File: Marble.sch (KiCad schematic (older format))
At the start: 16 parts

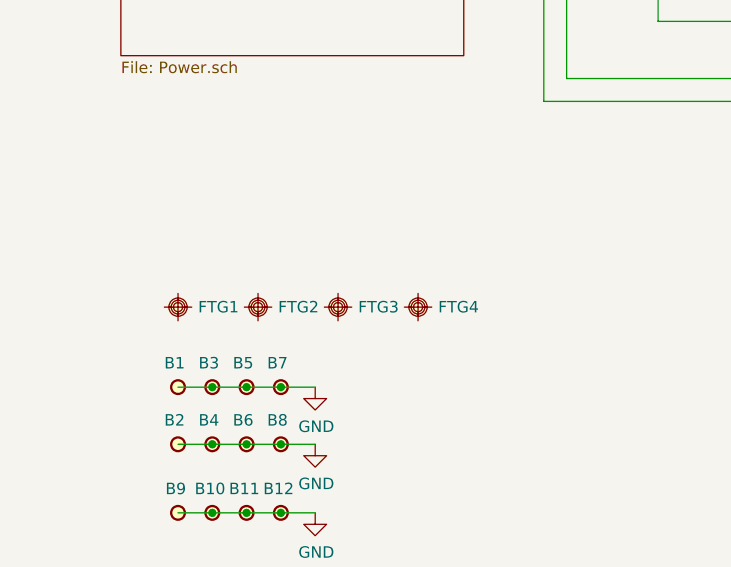
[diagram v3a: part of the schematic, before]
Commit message: 4 more fiducials
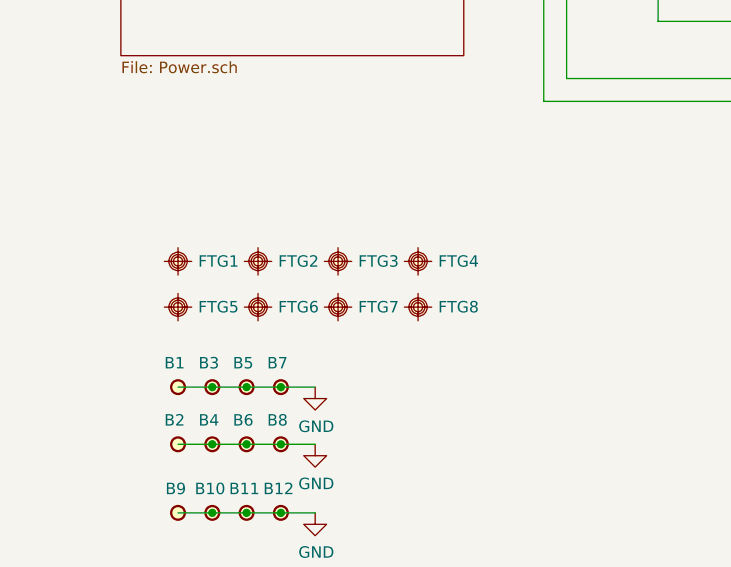
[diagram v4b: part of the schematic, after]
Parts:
- added FTG5, FTG7: FIDUCIAL_TARGET_C100-200, Pads:FIDUCIAL_BOT_S200-400, symbol Pads:FIDUCIAL_TARGET_C100-200
- added FTG6, FTG8: Pads:FIDUCIAL_BOT_S200-400, Pads:FIDUCIAL_BOT_S200-400, symbol Pads:FIDUCIAL_TARGET_C100-200
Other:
- moved on the sheet: FTG1, FTG2, FTG3, FTG4

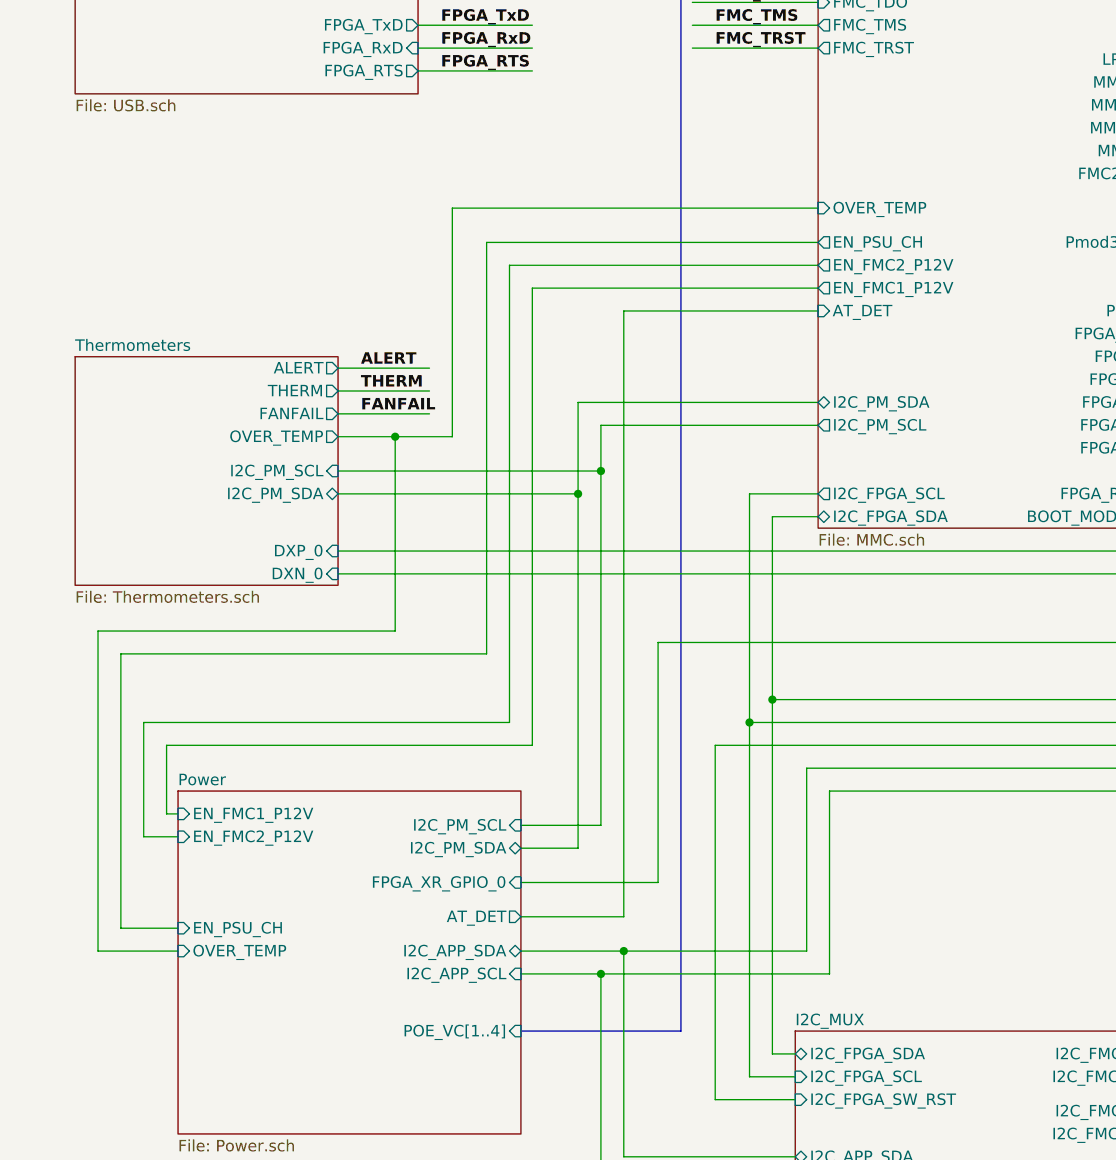
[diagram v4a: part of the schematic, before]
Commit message: reduced reels with components, DDR 1V5 enable signal connected to MMC, DDR I2C pull-ups powerd from 3.3VP
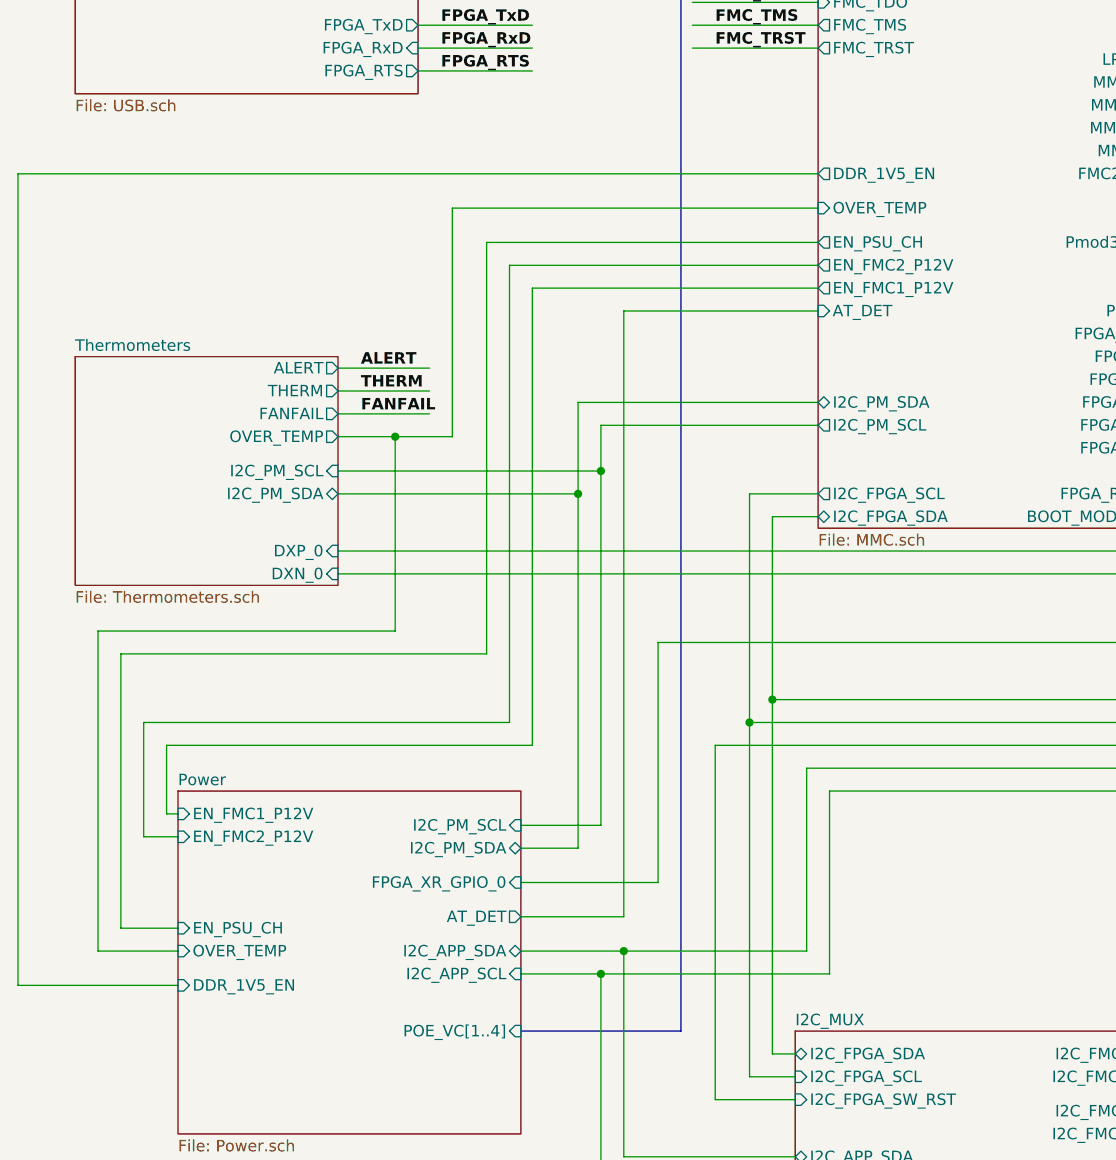
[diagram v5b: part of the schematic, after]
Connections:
- wire segments 358 -> 361
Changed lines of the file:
@@
 F11 "I2C_APP_SDA" B R 3900 12550 50
 F12 "I2C_APP_SCL" I R 3900 12650 50
+F13 "DDR_1V5_EN" I L 2400 12700 50
 $EndSheet
 $Sheet
@@
 F46 "MUX3_MMC" O L 5200 7350 50
 F47 "ISP_RSTn" U L 5200 8000 50
+F48 "DDR_1V5_EN" O L 5200 9150 50
 $EndSheet
 Text Label 6800 7550 0    50   ~ 10
@@
 	1    0    0    -1
 $EndComp
+Wire Wire Line
+	2400 12700 1700 12700
+Wire Wire Line
+	1700 12700 1700 9150
+Wire Wire Line
+	1700 9150 5200 9150
 $EndSCHEMATC

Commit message: Another attempt at fiducial clean-up
This time harmonize library, schematic, and layout.
Symbol name / layout value is FIDUCIAL_TARGET_R200-400
Needs checking.
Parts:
- FTG1, FTG2: value FIDUCIAL_TARGET_C100-200 -> FIDUCIAL_TARGET_R200-400; footprint Pads:FIDUCIAL_TOP_S200-400 -> Pads:FIDUCIAL_TARGET_R200-400; symbol Pads:FIDUCIAL_TARGET_C100-200 -> Pads:FIDUCIAL_TARGET_R200-400; Case ~~ -> (none); Comment ~~ -> (none); ComponentLink1Description ~~ -> (none); ComponentLink2Description ~~ -> (none); Database Table Name (none) -> Pads; Footprint Library (none) -> Pads; Footprint Ref FIDUCIAL_TOP_C100-200 -> FIDUCIAL_TARGET_R200-400; Library Name Pads -> Eletro-mechanical.DbLib; Manufacturer ~~ -> (none); Manufacturer Part Number ~~ -> (none); Manufacturer1 ComponentHeight ~~ -> (none); Manufacturer1 Example ~~ -> (none); Manufacturer1 Part Number ~~ -> (none); PackageDescription Round Fiducial Target, Top Layer, 1.0mm, Top Solder 2.0mm, 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 -> Round Fiducial Target, Top Layer, 2.0mm, Top Solder 4.0mm, 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; Part Description Round Fiducial Target, Top Layer, 1.0mm, Top Solder 2.0mm, 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 -> Round Fiducial Target, Top Layer, 2.0mm, Solder 4.0mm, Keep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; Part Number FIDUCIAL_TARGET_C100-200 -> FIDUCIAL_TARGET_R200-400; SCEM ~~ -> (none); Sense Comment ~~ -> (none); Status Comment ~~ -> (none)
- FTG3, FTG5, FTG7: value FIDUCIAL_TARGET_C100-200 -> FIDUCIAL_TARGET_R200-400; footprint Pads:FIDUCIAL_BOT_S200-400 -> Pads:FIDUCIAL_TARGET_R200-400; symbol Pads:FIDUCIAL_TARGET_C100-200 -> Pads:FIDUCIAL_TARGET_R200-400; Case ~~ -> (none); Comment ~~ -> (none); ComponentLink1Description ~~ -> (none); ComponentLink2Description ~~ -> (none); Database Table Name (none) -> Pads; Footprint Library (none) -> Pads; Footprint Ref FIDUCIAL_TOP_C100-200 -> FIDUCIAL_TARGET_R200-400; Library Name Pads -> Eletro-mechanical.DbLib; Manufacturer ~~ -> (none); Manufacturer Part Number ~~ -> (none); Manufacturer1 ComponentHeight ~~ -> (none); Manufacturer1 Example ~~ -> (none); Manufacturer1 Part Number ~~ -> (none); PackageDescription Round Fiducial Target, Top Layer, 1.0mm, Top Solder 2.0mm, 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 -> Round Fiducial Target, Top Layer, 2.0mm, Top Solder 4.0mm, 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; Part Description Round Fiducial Target, Top Layer, 1.0mm, Top Solder 2.0mm, 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 -> Round Fiducial Target, Top Layer, 2.0mm, Solder 4.0mm, Keep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; Part Number FIDUCIAL_TARGET_C100-200 -> FIDUCIAL_TARGET_R200-400; SCEM ~~ -> (none); Sense Comment ~~ -> (none); Status Comment ~~ -> (none)
- FTG4, FTG6, FTG8: value Pads:FIDUCIAL_BOT_S200-400 -> FIDUCIAL_TARGET_R200-400; footprint Pads:FIDUCIAL_BOT_S200-400 -> Pads:FIDUCIAL_TARGET_R200-400; symbol Pads:FIDUCIAL_TARGET_C100-200 -> Pads:FIDUCIAL_TARGET_R200-400; Case ~~ -> (none); Comment ~~ -> (none); ComponentLink1Description ~~ -> (none); ComponentLink2Description ~~ -> (none); Database Table Name (none) -> Pads; Footprint Library (none) -> Pads; Footprint Ref FIDUCIAL_TOP_C100-200 -> FIDUCIAL_TARGET_R200-400; Library Name Pads -> Eletro-mechanical.DbLib; Manufacturer ~~ -> (none); Manufacturer Part Number ~~ -> (none); Manufacturer1 ComponentHeight ~~ -> (none); Manufacturer1 Example ~~ -> (none); Manufacturer1 Part Number ~~ -> (none); PackageDescription Round Fiducial Target, Top Layer, 1.0mm, Top Solder 2.0mm, 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 -> Round Fiducial Target, Top Layer, 2.0mm, Top Solder 4.0mm, 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; Part Description Round Fiducial Target, Top Layer, 1.0mm, Top Solder 2.0mm, 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 -> Round Fiducial Target, Top Layer, 2.0mm, Solder 4.0mm, Keep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; Part Number FIDUCIAL_TARGET_C100-200 -> FIDUCIAL_TARGET_R200-400; SCEM ~~ -> (none); Sense Comment ~~ -> (none); Status Comment ~~ -> (none)

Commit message: new hole for mounting holes, new PN for D6 and D7
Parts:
- B1, B2, B3, B4, B5, B6, B7, B8: value PLATED_HOLE2.7_PAD5.0 -> PLATED_HOLE3.0_PAD5.0; footprint Pads:MTG270_500 -> Pads:MTG300_500; symbol Pads:PLATED_HOLE2.7_PAD5.0 -> Pads:PLATED_HOLE3.0_PAD5.0; Case ~~ -> (none); Comment ~~ -> (none); ComponentLink1Description ~~ -> (none); ComponentLink2Description ~~ -> (none); Database Table Name (none) -> Pads; Footprint Library (none) -> Pads; Footprint Ref MTG270_500 -> MTG300_500; Library Name Pads -> Eletro-mechanical.DbLib; Manufacturer ~~ -> (none); Manufacturer Part Number ~~ -> (none); Manufacturer1 ComponentHeight ~~ -> (none); Manufacturer1 Example ~~ -> (none); Manufacturer1 Part Number ~~ -> (none); Part Number PLATED_HOLE2.7_PAD5.0 -> PLATED_HOLE3.0_PAD5.0; SCEM ~~ -> (none); Sense Comment ~~ -> (none); Status Comment ~~ -> (none)
- B10, B11, B12, B9: value PLATED_HOLE3.0_PAD6.0 -> PLATED_HOLE3.0_PAD5.0; footprint Pads:MTG300_600 -> Pads:MTG300_500; symbol Pads:PLATED_HOLE3.0_PAD6.0 -> Pads:PLATED_HOLE3.0_PAD5.0; Author CERN DEM JLC -> CERN DEM JMW; CreateDate 05/26/08 00:00:00 -> 09/27/11 00:00:00; Footprint Ref MTG300_600 -> MTG300_500; LatestRevisionDate 05/26/08 00:00:00 -> 09/27/11 00:00:00; PackageDescription Plated Through Hole: Hole Dia.=3.0mm Pad Dia.=6.0mm -> Plated Through Hole: Hole Dia.=2.7mm Pad Dia.=5.0mm; Part Description Plated Through Hole: Hole Dia.=3.0mm Pad Dia.=6.0mm -> Plated Through Hole: Hole Dia.=2.7mm Pad Dia.=5.0mm; Part Number PLATED_HOLE3.0_PAD6.0 -> PLATED_HOLE3.0_PAD5.0
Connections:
- wire segments 361 -> 349

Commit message: More mounting hole work
Re-attach mounting holes to ground on schematic
Change all footprint names and sizes in layout to 3mm hole dia, 5mm pad dia
Configure KiBOM to not include them in BOM output
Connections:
- wire segments 349 -> 361
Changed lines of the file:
@@
 Wire Wire Line
 	1700 9150 5200 9150
+Wire Wire Line
+	2650 14800 2800 14800
+Connection ~ 2800 14800
+Wire Wire Line
+	2800 14800 2950 14800
+Connection ~ 2950 14800
+Wire Wire Line
+	2950 14800 3100 14800
+Connection ~ 3100 14800
+Wire Wire Line
+	3100 14800 3250 14800
+Wire Wire Line
+	2650 15050 2800 15050
+Connection ~ 2800 15050
+Wire Wire Line
+	2800 15050 2950 15050
+Connection ~ 2950 15050
+Wire Wire Line
+	2950 15050 3100 15050
+Connection ~ 3100 15050
+Wire Wire Line
+	3100 15050 3250 15050
+Wire Wire Line
+	2650 15350 2800 15350
+Connection ~ 2800 15350
+Wire Wire Line
+	2800 15350 2950 15350
+Connection ~ 2950 15350
+Wire Wire Line
+	2950 15350 3100 15350
+Connection ~ 3100 15350
+Wire Wire Line
+	3100 15350 3250 15350
 $EndSCHEMATC
